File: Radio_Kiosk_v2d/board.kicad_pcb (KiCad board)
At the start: 4 copper layers, 85 x 120 mm, 239 parts, among them J1 USB-C PD in, J11 UART, J12 USB-C, J13 Lid LEDs, J2 DC in 18-26V, PJ-002BH 5.5x2.5, J3 Laptop out 15.6V, PJ-002BH 5.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, J5 RJ45 radio, J6 RJ45 laptop, J8 Fan 12V, J9 SWD, Q1 SI4470EY, Q10 2N7002, Q11 AO3400A, Q12 SI4470EY, Q13 AO4482, Q2 SI4470EY, Q20 AO4482, Q22 PSMN075-100MSEX, Q23 DMP10H400SE, Q24 BSS123, Q25 2N7002, Q30 AO3400A, Q40 AOD4184A, Q41 AOD4184A, Q44 SI4401DDY, Q45 2N7002, Q6 SI4470EY, Q7 SI4470EY, Q8 AOD4185, Q9 2N7002, SW1 RESET, SW2 BOOT0 (DFU), U1 LM74700-Q1, U10 TLV7011, U12 LM74700-Q1, U2 LM74700-Q1, U20 LM3478 54V boost, U21 TPS26600 eFuse, U22 LTC4279, U3 LMR33630 12V, U30 SN74AHCT1G125, U31 SN74AHCT1G125, U4 LM3150 15.75V 4.5A, U40 STM32F072CBT6, U41 INA180A1, U42 INA180A1, U43 MCP6001T-I/OT, U45 TLV7011, U5 LMR33630 5V, U50 CH224A, U51 AP2112K-3.3, U52 USBLC6-2SC6, U6 LM74700-Q1, U7 LM74700-Q1

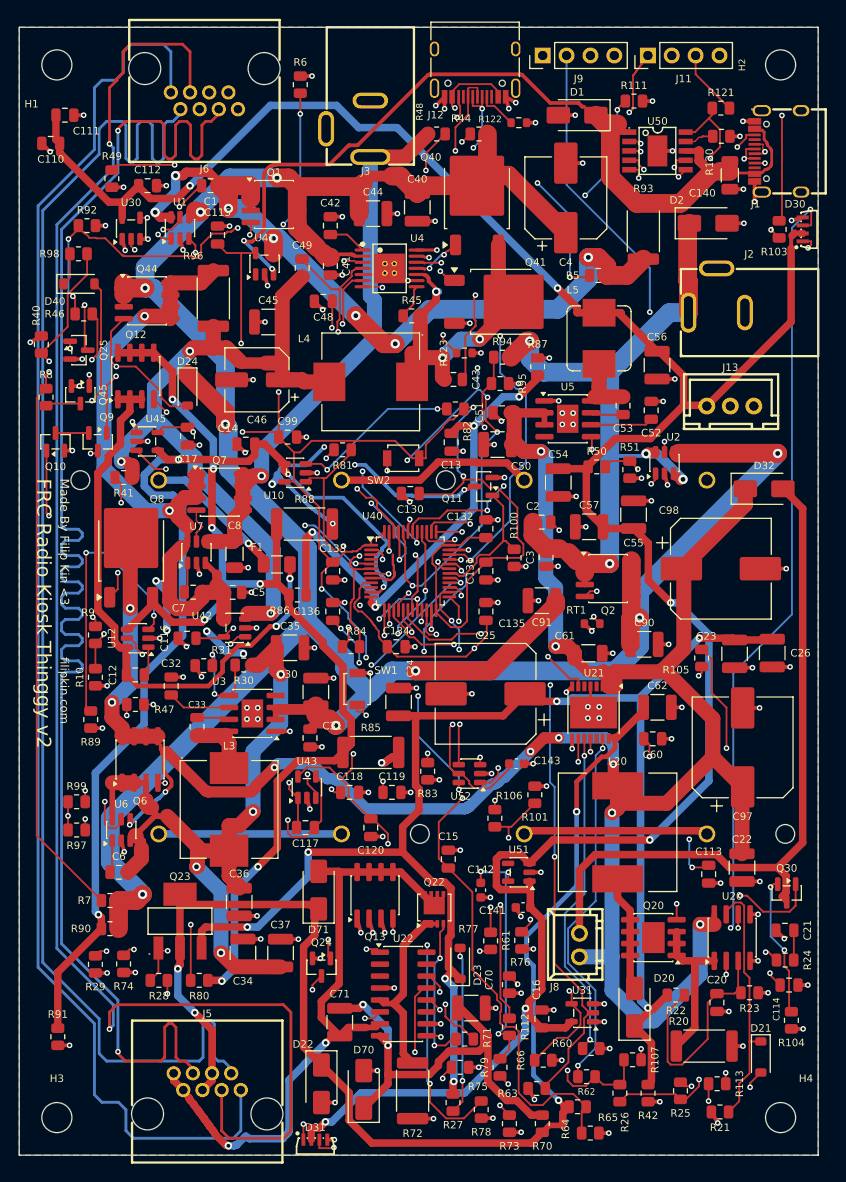
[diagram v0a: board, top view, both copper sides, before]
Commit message: v2d: fully routed, nothing foreign under the inductors, fab files
- Copper under L3/L4/L5/L20 ripped and re-routed with a keep-out: no signal on
  any layer, no foreign net on F.Cu or In2; power may pass on B.Cu under the
  In1 plane (FAN_N under L20 does).
- Last open net closed by a pin swap: USB_ISENSE PA0 -> PA3, PORT_SW PA3 ->
  PC15; schematic and firmware regenerated.
- KiCad DRC: 0 unconnected, no copper errors. fab/: gerbers, drill, JLC BOM
  and CPL.

Co-Authored-By: Claude Opus 5.5 <noreply@anthropic.com>
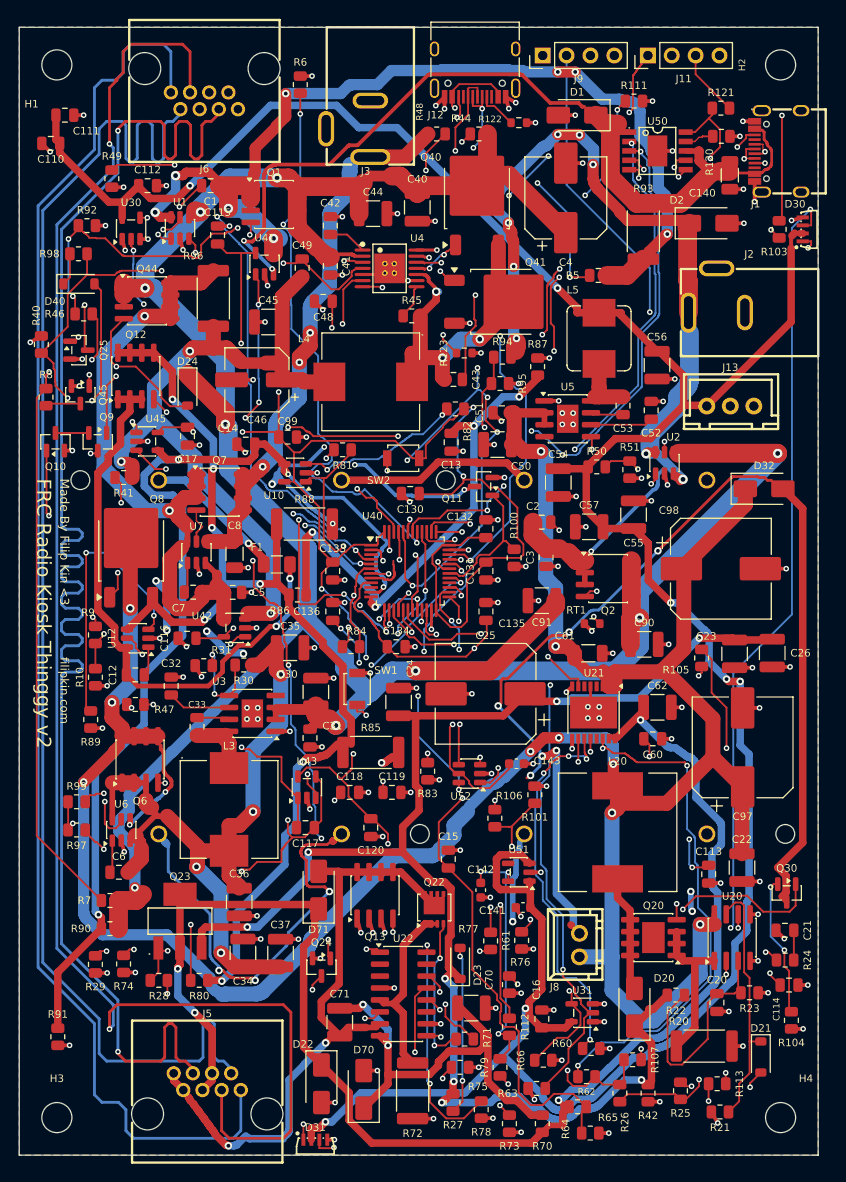
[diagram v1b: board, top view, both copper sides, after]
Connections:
- U40 pad 10: USB_ISENSE -> (no net)
- U40 pad 13: PORT_SW -> USB_ISENSE
- U40 pad 4: (no net) -> PORT_SW
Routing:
- net USB_ISENSE: track 0.00 -> 50.7 mm, vias 0 -> 6
- net FAN_N: track 75.7 -> 119.0 mm, vias 0 -> 6
- net +12V: track 249.6 -> 284.9 mm
- net +5V: track 263.2 -> 297.6 mm, vias 6 -> 7
- net PACK_1: track 19.4 -> 43.6 mm, vias 0 -> 3
- net LED_DATA: track 80.7 -> 57.3 mm, vias 3 -> 5
- net VIN_USBS: track 79.9 -> 102.0 mm, vias 7 -> 8
- net PORT_SW: track 65.9 -> 87.4 mm, vias 3 -> 7
- net VIN_DC: track 77.9 -> 98.3 mm, vias 4 -> 9
- net PACK_3: track 19.7 -> 37.6 mm, vias 0 -> 3
- net U4_FB: track 80.3 -> 65.1 mm, vias 3 -> 4
- net PASSIVE_FLT: track 63.4 -> 77.6 mm, vias 3 -> 4
- net LAPTOP_OK: track 82.2 -> 94.1 mm, vias 3 -> 5
- net PORT_P: track 141.7 -> 152.4 mm
- net USB_DP_CON: track 82.9 -> 91.6 mm
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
